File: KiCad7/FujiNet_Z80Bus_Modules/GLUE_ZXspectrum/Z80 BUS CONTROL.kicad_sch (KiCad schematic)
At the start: 9 parts, among them IC6 74HC32N, IC7 74HC32N

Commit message: GLUE is broken again, logic gate annotation issue
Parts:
- renumbered D3 to D?, D4 to D?, IC6 to IC?, IC7 to IC?, R12 to R5, R13 to R6
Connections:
- net ESP_CONTROL.MEMRQ: now also IC?.13; no longer IC?.5
- net ESP_CONTROL.WR: now also IC?.4; no longer IC?.9
- net ESP_IOD_CONFIG: now also IC?.12; no longer IC?.4
- net PERM_Z80_IORQ: now also IC?.2, IC?.5; no longer IC?.13, IC?.5
- net Z80_ADD_CONNECT: now also IC?.9; no longer IC?.1
- net Z80_BUS_CONTROL.Z80_ADD_DIR: now also IC?.11; no longer IC?.6
- net Z80_BUS_CONTROL.Z80_ADD_OE: now also IC?.8; no longer IC?.3
- net Z80_BUS_CONTROL.Z80_DATA_DIR: now also IC?.3; no longer IC?.8
- net Z80_BUS_CONTROL.Z80_DATA_OE: now also IC?.6; no longer IC?.11
- net Z80_CONTROL.RD: now also IC?.1; no longer IC?.4
- net Z80_DATA_CONNECT: now also IC?.4, IC?.5; no longer IC?.10, IC?.12
- net at IC?.3: now also IC?.10; no longer IC?.2
- new net: IC?.2, IC?.6
- new net: IC?.1, IC?.3

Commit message: KiCad FIXED GLUE
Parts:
- removed Q?: 2N2222 (BC337), Package_TO_SOT_THT:TO-92, symbol Transistor_BJT:BC337
- removed R? (x2): 1K, Resistor_THT:R_Axial_DIN0207_L6.3mm_D2.5mm_P10.16mm_Horizontal, symbol Device:R
- added IC?: 7404N, Package_DIP:DIP-14_W7.62mm_Socket, symbol 74xx:74HC04
- renumbered R5 to R3, R6 to R4
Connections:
- net !CACHE_DATASTATUS: now also IC?.2
- net CACHE_DATASTATUS: now also IC?.1
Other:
- note removed: "There is a NOT gate on IC4 that can replace this now"

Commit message: KiCad Adapter Concept v2 pcb draft layout
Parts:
- renumbered R3 to R5, R4 to R6
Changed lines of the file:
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@@
     (pin "7")
     (instances
-      (project "FujiNet_Z80Bus_ReferenceDesign"
+      (project "ZXspectrum_Concept_v2.kicad_pro"
         (path "/532c0392-800e-45cc-8170-6d32f2390e83"
           (reference "IC?") (unit 2)
         )
-        (path "/532c0392-800e-45cc-8170-6d32f2390e83/6a1fd481-1635-4a64-b244-c204161ad407/6bcd45ec-1810-4278-8058-96e26ec9b5f3"
-          (reference "IC?") (unit 2)
+        (path "/532c0392-800e-45cc-8170-6d32f2390e83/95233ba0-af33-48c6-a370-2e3f14ae4dcf/6bcd45ec-1810-4278-8058-96e26ec9b5f3"
+          (reference "IC5") (unit 2)
         )
       )
@@
     (pin "1")
     (instances
-      (project "FujiNet_Z80Bus_ReferenceDesign"
-        (path "/532c0392-800e-45cc-8170-6d32f2390e83/6a1fd481-1635-4a64-b244-c204161ad407/6bcd45ec-1810-4278-8058-96e26ec9b5f3"
+      (project "ZXspectrum_Concept_v2.kicad_pro"
+        (path "/532c0392-800e-45cc-8170-6d32f2390e83/95233ba0-af33-48c6-a370-2e3f14ae4dcf/6bcd45ec-1810-4278-8058-96e26ec9b5f3"
           (reference "#PWR0106") (unit 1)
         )
@@
     (pin "7")
     (instances
-      (project "FujiNet_Z80Bus_ReferenceDesign"
-        (path "/532c0392-800e-45cc-8170-6d32f2390e83"
-          (reference "IC?") (unit 1)
-        )
-        (path "/532c0392-800e-45cc-8170-6d32f2390e83/6a1fd481-1635-4a64-b244-c204161ad407/6bcd45ec-1810-4278-8058-96e26ec9b5f3"
-          (reference "IC?") (unit 1)
+      (project "ZXspectrum_Concept_v2.kicad_pro"
+        (path "/532c0392-800e-45cc-8170-6d32f2390e83"
+          (reference "IC?") (unit 1)
+        )
+        (path "/532c0392-800e-45cc-8170-6d32f2390e83/95233ba0-af33-48c6-a370-2e3f14ae4dcf/6bcd45ec-1810-4278-8058-96e26ec9b5f3"
+          (reference "IC9") (unit 1)
         )
       )
@@
     (pin "7")
     (instances
-      (project "FujiNet_Z80Bus_ReferenceDesign"
-        (path "/532c0392-800e-45cc-8170-6d32f2390e83"
-          (reference "IC?") (unit 1)
-        )
-        (path "/532c0392-800e-45cc-8170-6d32f2390e83/6a1fd481-1635-4a64-b244-c204161ad407/6bcd45ec-1810-4278-8058-96e26ec9b5f3"
-          (reference "IC?") (unit 1)
+      (project "ZXspectrum_Concept_v2.kicad_pro"
+        (path "/532c0392-800e-45cc-8170-6d32f2390e83"
+          (reference "IC?") (unit 1)
+        )
+        (path "/532c0392-800e-45cc-8170-6d32f2390e83/95233ba0-af33-48c6-a370-2e3f14ae4dcf/6bcd45ec-1810-4278-8058-96e26ec9b5f3"
+          (reference "IC7") (unit 1)
         )
       )
@@
     (pin "7")
     (instances
-      (project "FujiNet_Z80Bus_ReferenceDesign"
-        (path "/532c0392-800e-45cc-8170-6d32f2390e83"
-          (reference "IC?") (unit 1)
-        )
-        (path "/532c0392-800e-45cc-8170-6d32f2390e83/6a1fd481-1635-4a64-b244-c204161ad407/6bcd45ec-1810-4278-8058-96e26ec9b5f3"
-          (reference "IC?") (unit 1)
+      (project "ZXspectrum_Concept_v2.kicad_pro"
+        (path "/532c0392-800e-45cc-8170-6d32f2390e83"
+          (reference "IC?") (unit 1)
+        )
+        (path "/532c0392-800e-45cc-8170-6d32f2390e83/95233ba0-af33-48c6-a370-2e3f14ae4dcf/6bcd45ec-1810-4278-8058-96e26ec9b5f3"
+          (reference "IC1") (unit 5)
         )
       )
@@
     (pin "2")
     (instances
-      (project "FujiNet_Z80Bus_ReferenceDesign"
+      (project "ZXspectrum_Concept_v2.kicad_pro"
         (path "/532c0392-800e-45cc-8170-6d32f2390e83"
           (reference "D?") (unit 1)
         )
-        (path "/532c0392-800e-45cc-8170-6d32f2390e83/6a1fd481-1635-4a64-b244-c204161ad407/6bcd45ec-1810-4278-8058-96e26ec9b5f3"
+        (path "/532c0392-800e-45cc-8170-6d32f2390e83/95233ba0-af33-48c6-a370-2e3f14ae4dcf/6bcd45ec-1810-4278-8058-96e26ec9b5f3"
+          (reference "D7") (unit 1)
+        )
+      )
+      (project "GLUE_ZXspectrum"
+        (path "/648e0b91-567a-4972-a379-57b42123c6d5/6bcd45ec-1810-4278-8058-96e26ec9b5f3"
           (reference "D?") (unit 1)
         )
       )
-      (project "GLUE_ZXspectrum"
-        (path "/648e0b91-567a-4972-a379-57b42123c6d5/6bcd45ec-1810-4278-8058-96e26ec9b5f3"
-          (reference "D?") (unit 1)
-        )
-      )
     )
   )
@@
     (pin "7")
     (instances
-      (project "FujiNet_Z80Bus_ReferenceDesign"
+      (project "ZXspectrum_Concept_v2.kicad_pro"
         (path "/532c0392-800e-45cc-8170-6d32f2390e83"
           (reference "IC?") (unit 2)
         )
-        (path "/532c0392-800e-45cc-8170-6d32f2390e83/6a1fd481-1635-4a64-b244-c204161ad407/6bcd45ec-1810-4278-8058-96e26ec9b5f3"
-          (reference "IC?") (unit 2)
+        (path "/532c0392-800e-45cc-8170-6d32f2390e83/95233ba0-af33-48c6-a370-2e3f14ae4dcf/6bcd45ec-1810-4278-8058-96e26ec9b5f3"
+          (reference "IC7") (unit 2)
         )
       )
@@
   (symbol (lib_id "Device:R") (at 86.36 135.89 90) (unit 1)
     (in_bom yes) (on_board yes) (dnp no)
-    (property "Reference" "R4" (at 86.36 133.35 90)
+    (property "Reference" "R6" (at 86.36 133.35 90)
       (effects (font (size 1.27 1.27)))
     )
@@
     (pin "2")
     (instances
-      (project "FujiNet_Z80Bus_ReferenceDesign"
-        (path "/532c0392-800e-45cc-8170-6d32f2390e83/6a1fd481-1635-4a64-b244-c204161ad407/6bcd45ec-1810-4278-8058-96e26ec9b5f3"
-          (reference "R4") (unit 1)
+      (project "ZXspectrum_Concept_v2.kicad_pro"
+        (path "/532c0392-800e-45cc-8170-6d32f2390e83/95233ba0-af33-48c6-a370-2e3f14ae4dcf/6bcd45ec-1810-4278-8058-96e26ec9b5f3"
+          (reference "R6") (unit 1)
         )
       )
@@
     (pin "7")
     (instances
-      (project "FujiNet_Z80Bus_ReferenceDesign"
-        (path "/532c0392-800e-45cc-8170-6d32f2390e83"
-          (reference "IC?") (unit 1)
-        )
-        (path "/532c0392-800e-45cc-8170-6d32f2390e83/6a1fd481-1635-4a64-b244-c204161ad407/6bcd45ec-1810-4278-8058-96e26ec9b5f3"
-          (reference "IC?") (unit 1)
+      (project "ZXspectrum_Concept_v2.kicad_pro"
+        (path "/532c0392-800e-45cc-8170-6d32f2390e83"
+          (reference "IC?") (unit 1)
+        )
+        (path "/532c0392-800e-45cc-8170-6d32f2390e83/95233ba0-af33-48c6-a370-2e3f14ae4dcf/6bcd45ec-1810-4278-8058-96e26ec9b5f3"
+          (reference "IC9") (unit 2)
         )
       )
@@
   (symbol (lib_id "Device:R") (at 86.36 68.58 270) (unit 1)
     (in_bom yes) (on_board yes) (dnp no) (fields_autoplaced)
-    (property "Reference" "R3" (at 86.36 63.5 90)
+    (property "Reference" "R5" (at 86.36 63.5 90)
       (effects (font (size 1.27 1.27)))
     )
@@
     (pin "2")
     (instances
-      (project "FujiNet_Z80Bus_ReferenceDesign"
-        (path "/532c0392-800e-45cc-8170-6d32f2390e83/6a1fd481-1635-4a64-b244-c204161ad407/6bcd45ec-1810-4278-8058-96e26ec9b5f3"
-          (reference "R3") (unit 1)
+      (project "ZXspectrum_Concept_v2.kicad_pro"
+        (path "/532c0392-800e-45cc-8170-6d32f2390e83/95233ba0-af33-48c6-a370-2e3f14ae4dcf/6bcd45ec-1810-4278-8058-96e26ec9b5f3"
+          (reference "R5") (unit 1)
         )
       )
@@
     (pin "7")
     (instances
-      (project "FujiNet_Z80Bus_ReferenceDesign"
+      (project "ZXspectrum_Concept_v2.kicad_pro"
         (path "/532c0392-800e-45cc-8170-6d32f2390e83"
           (reference "IC?") (unit 3)
         )
-        (path "/532c0392-800e-45cc-8170-6d32f2390e83/6a1fd481-1635-4a64-b244-c204161ad407/6bcd45ec-1810-4278-8058-96e26ec9b5f3"
-          (reference "IC?") (unit 3)
+        (path "/532c0392-800e-45cc-8170-6d32f2390e83/95233ba0-af33-48c6-a370-2e3f14ae4dcf/6bcd45ec-1810-4278-8058-96e26ec9b5f3"
+          (reference "IC9") (unit 3)
         )
       )
@@
     (pin "7")
     (instances
-      (project "FujiNet_Z80Bus_ReferenceDesign"
+      (project "ZXspectrum_Concept_v2.kicad_pro"
         (path "/532c0392-800e-45cc-8170-6d32f2390e83"
           (reference "IC?") (unit 4)
         )
-        (path "/532c0392-800e-45cc-8170-6d32f2390e83/6a1fd481-1635-4a64-b244-c204161ad407/6bcd45ec-1810-4278-8058-96e26ec9b5f3"
-          (reference "IC?") (unit 4)
+        (path "/532c0392-800e-45cc-8170-6d32f2390e83/95233ba0-af33-48c6-a370-2e3f14ae4dcf/6bcd45ec-1810-4278-8058-96e26ec9b5f3"
+          (reference "IC9") (unit 4)
         )
       )
@@
     (pin "2")
     (instances
-      (project "FujiNet_Z80Bus_ReferenceDesign"
+      (project "ZXspectrum_Concept_v2.kicad_pro"
         (path "/532c0392-800e-45cc-8170-6d32f2390e83"
           (reference "D?") (unit 1)
         )
-        (path "/532c0392-800e-45cc-8170-6d32f2390e83/6a1fd481-1635-4a64-b244-c204161ad407/6bcd45ec-1810-4278-8058-96e26ec9b5f3"
-          (reference "D?") (unit 1)
+        (path "/532c0392-800e-45cc-8170-6d32f2390e83/95233ba0-af33-48c6-a370-2e3f14ae4dcf/6bcd45ec-1810-4278-8058-96e26ec9b5f3"
+          (reference "D8") (unit 1)
         )
       )
@@
     (pin "1")
     (instances
-      (project "FujiNet_Z80Bus_ReferenceDesign"
-        (path "/532c0392-800e-45cc-8170-6d32f2390e83/6a1fd481-1635-4a64-b244-c204161ad407/6bcd45ec-1810-4278-8058-96e26ec9b5f3"
+      (project "ZXspectrum_Concept_v2.kicad_pro"
+        (path "/532c0392-800e-45cc-8170-6d32f2390e83/95233ba0-af33-48c6-a370-2e3f14ae4dcf/6bcd45ec-1810-4278-8058-96e26ec9b5f3"
           (reference "#PWR0107") (unit 1)
         )

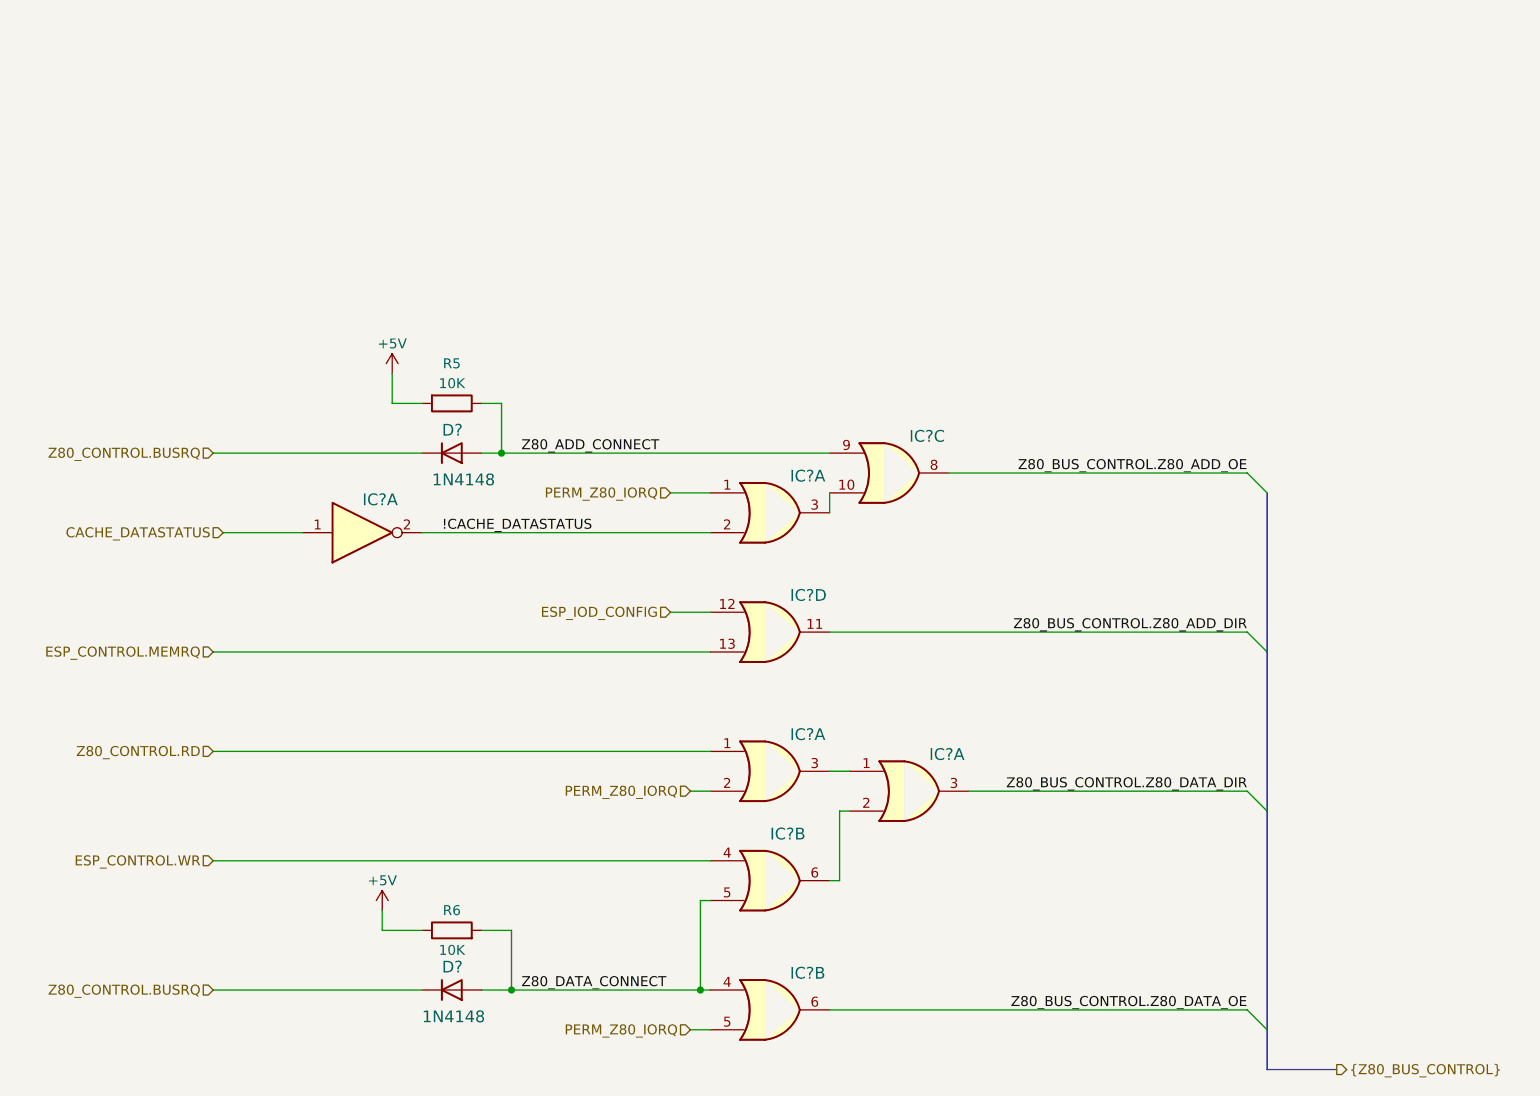
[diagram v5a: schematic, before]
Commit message: KiCad - Fixed GLUE (need to update concept v2)
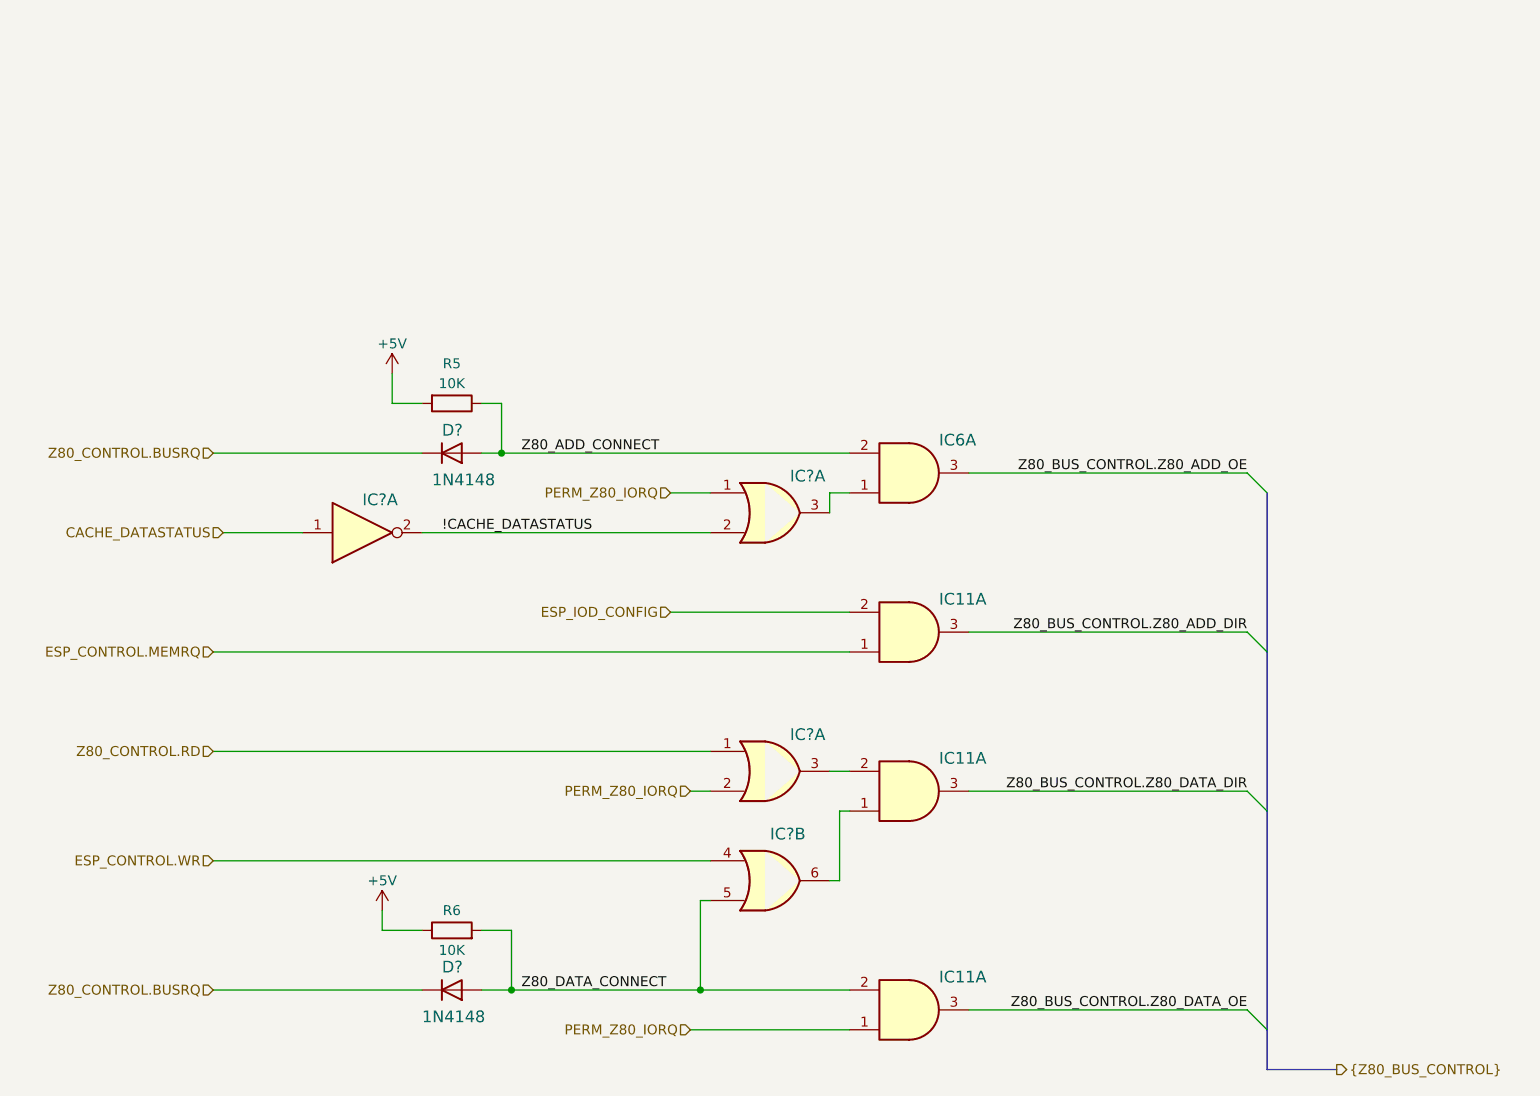
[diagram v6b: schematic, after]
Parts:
- removed IC? (x4): 74HC32N, Package_DIP:DIP-14_W7.62mm_Socket, symbol 74xx:74LS32
- added IC11 (x3), IC6: 74HC08N, Package_DIP:DIP-14_W7.62mm_Socket, symbol 74xx:74LS08
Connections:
- net ESP_CONTROL.MEMRQ: now also IC11.1
- net ESP_IOD_CONFIG: now also IC11.2
- net PERM_Z80_IORQ: now also IC11.1
- net Z80_ADD_CONNECT: now also IC6.2
- net Z80_BUS_CONTROL.Z80_ADD_DIR: now also IC11.3
- net Z80_BUS_CONTROL.Z80_ADD_OE: now also IC6.3
- net Z80_BUS_CONTROL.Z80_DATA_DIR: now also IC11.3
- net Z80_BUS_CONTROL.Z80_DATA_OE: now also IC11.3
- net Z80_DATA_CONNECT: now also IC11.2
- net at IC?.6: now also IC11.1
- net at IC?.3: now also IC11.2
- net at IC?.3: now also IC6.1
